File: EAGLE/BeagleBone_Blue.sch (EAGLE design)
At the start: 302 parts, among them J2 SERVO_HEADERS_8X, M1 JST_ZH_2, M2 JST_ZH_2, M3 JST_ZH_2, M4 JST_ZH_2, Q1 MOSFET-N, U1 TCAN1051HV, U10 TXS0108ERGYR, U13 EMMC, U2 SN74LV1T126DBVR, U3 TPD4S012DRY, U4 TPD4S012DRY, U5 24LC_32AT-I/OT, U6 SN74LVC1G07_DCK_5, U7 WL1835MODGBMOCT, U9 TXS0108ERGYR, X2 SCHA5B0200, X3 USB1, X4 10118192-0001LF, Y1 24 MHz, Y2 32.768kHz

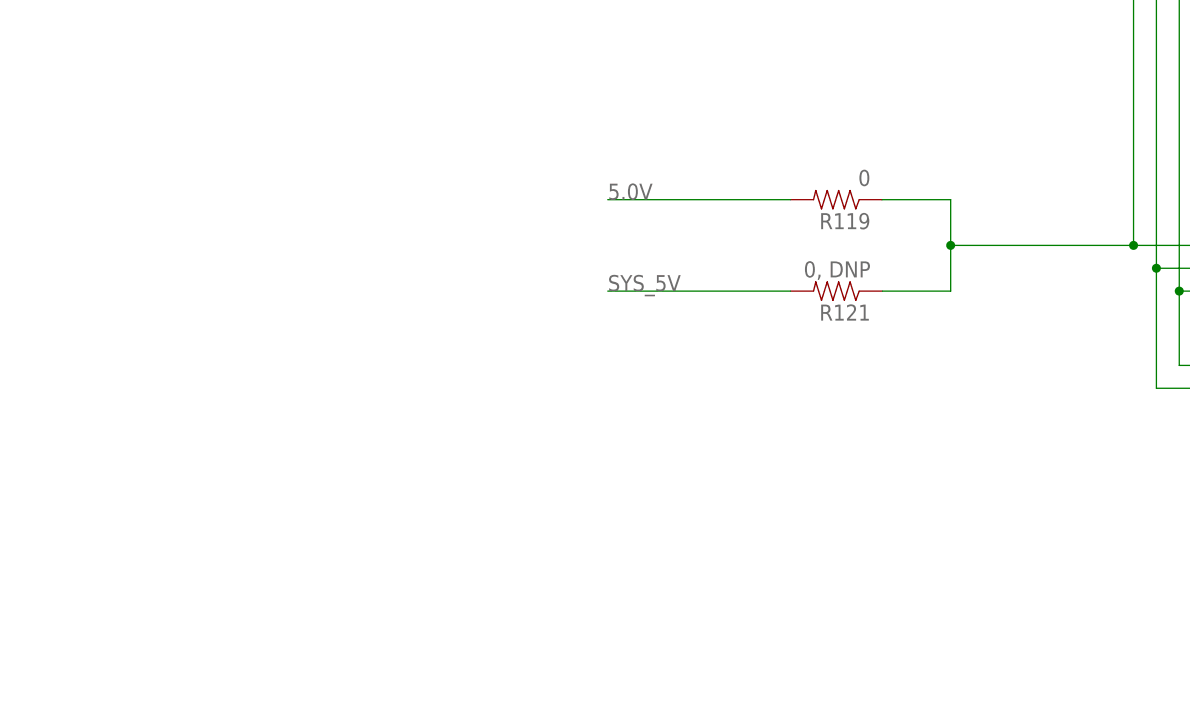
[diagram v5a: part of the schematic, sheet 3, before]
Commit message: Added TPS2105 power mux for USB1 power.
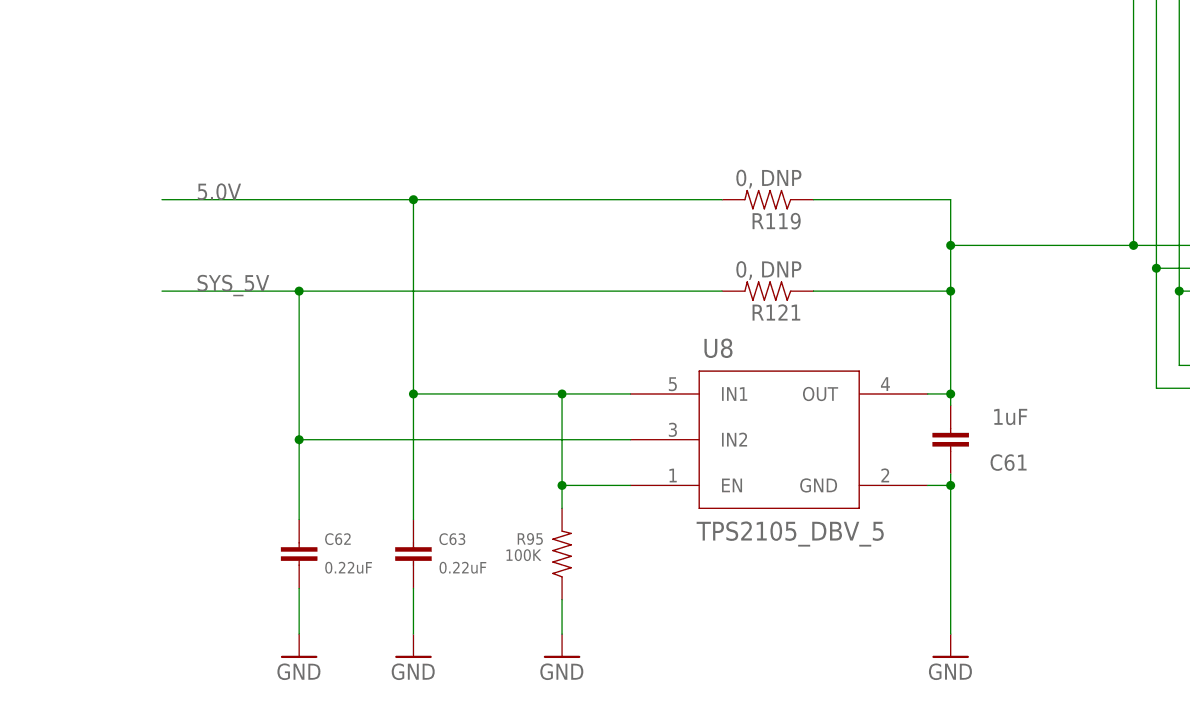
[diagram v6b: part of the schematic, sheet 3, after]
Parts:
- added C61: 1uF, Strawson_Eagle_Lib:CAP0402-CAP
- added C62, C63: 0.22uF, Strawson_Eagle_Lib:CAP0402-CAP
- added R95: 100K, Strawson_Eagle_Lib:RESISTOR0402-RES
- added U8: TPS2105_DBV_5, BeagleBone_Blue:TPS2105_DBV_5
- R119: value 0 -> 0, DNP
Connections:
- net 5.0V: now also C63.1, R95.2, U8.EN, U8.IN1
- net GND: now also C61.1, C62.2, C63.2, R95.1, U8.GND
- net SYS_5V: now also C62.1, U8.IN2
- net USB1_VBUS: now also C61.2, U8.OUT
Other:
- moved on the sheet: R119, R121
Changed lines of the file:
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@@
 <setting verticaltext="up"/>
 </settings>
-<grid distance="0.05" unitdist="inch" unit="inch" style="lines" multiple="1" display="no" altdistance="0.005" altunitdist="inch" altunit="inch"/>
+<grid distance="0.05" unitdist="inch" unit="inch" style="lines" multiple="1" display="no" altdistance="0.01" altunitdist="inch" altunit="inch"/>
 <layers>
 <layer number="1" name="Top" color="4" fill="1" visible="no" active="no"/>
@@
 <part name="R108" library="Strawson_Eagle_Lib" deviceset="RESISTOR" device="0402-RES" value="1K, DNP"/>
 <part name="R104" library="SparkFun-Resistors" deviceset="RESISTOR" device="0603" value="120, DNP"/>
-<part name="R119" library="SparkFun-Resistors" deviceset="RESISTOR" device="0603" value="0"/>
+<part name="R119" library="SparkFun-Resistors" deviceset="RESISTOR" device="0603" value="0, DNP"/>
 <part name="R121" library="SparkFun-Resistors" deviceset="RESISTOR" device="0603" value="0, DNP"/>
 <part name="Y2" library="GHI2" deviceset="CRYSTAL_3.2X1.5" device="" value="32.768kHz"/>
@@
 <part name="C59" library="SparkFun-Capacitors" deviceset="CAP" device="0805" value="10uF"/>
 <part name="C60" library="SparkFun-Capacitors" deviceset="CAP" device="0805" value="10uF"/>
+<part name="U8" library="BeagleBone_Blue" deviceset="TPS2105_DBV_5" device=""/>
+<part name="GND60" library="supply1" deviceset="GND" device=""/>
+<part name="R95" library="Strawson_Eagle_Lib" deviceset="RESISTOR" device="0402-RES" value="100K"/>
+<part name="GND61" library="supply1" deviceset="GND" device=""/>
+<part name="C61" library="Strawson_Eagle_Lib" deviceset="CAP" device="0402-CAP" value="1uF"/>
+<part name="C62" library="Strawson_Eagle_Lib" deviceset="CAP" device="0402-CAP" value="0.22uF"/>
+<part name="C63" library="Strawson_Eagle_Lib" deviceset="CAP" device="0402-CAP" value="0.22uF"/>
+<part name="GND62" library="supply1" deviceset="GND" device=""/>
+<part name="GND63" library="supply1" deviceset="GND" device=""/>
 </parts>
 <sheets>
@@
 <attribute name="VALUE" x="264.414" y="39.116" size="1.778" layer="96"/>
 </instance>
-<instance part="R119" gate="G$1" x="193.04" y="66.04" rot="R180"/>
-<instance part="R121" gate="G$1" x="193.04" y="55.88" rot="R180"/>
+<instance part="R119" gate="G$1" x="185.42" y="66.04" rot="R180"/>
+<instance part="R121" gate="G$1" x="185.42" y="55.88" rot="R180"/>
 <instance part="X4" gate="G$1" x="337.82" y="104.14" smashed="yes">
 <attribute name="NAME" x="332.74" y="115.57" size="1.778" layer="95" font="vector"/>
@@
 <instance part="SUPPLY85" gate="G$1" x="339.09" y="73.66" rot="R180"/>
 <instance part="R112" gate="G$1" x="326.39" y="127" rot="R180"/>
+<instance part="U8" gate="A" x="160.02" y="41.91"/>
+<instance part="GND60" gate="1" x="205.74" y="15.24"/>
+<instance part="R95" gate="G$1" x="162.56" y="26.67" smashed="yes" rot="R90">
+<attribute name="NAME" x="157.48" y="28.3464" size="1.27" layer="95" rot="R180" align="center-right"/>
+<attribute name="VALUE" x="156.21" y="26.543" size="1.27" layer="96" align="center-left"/>
+</instance>
+<instance part="GND61" gate="1" x="162.56" y="15.24"/>
+<instance part="C61" gate="G$1" x="205.74" y="40.64" smashed="yes" rot="R180">
+<attribute name="NAME" x="214.376" y="37.719" size="1.778" layer="95" rot="R180"/>
+<attribute name="VALUE" x="214.376" y="42.799" size="1.778" layer="96" rot="R180"/>
+</instance>
+<instance part="C62" gate="G$1" x="133.35" y="25.4" smashed="yes">
+<attribute name="NAME" x="136.144" y="27.686" size="1.27" layer="95"/>
+<attribute name="VALUE" x="136.144" y="24.511" size="1.27" layer="96"/>
+</instance>
+<instance part="C63" gate="G$1" x="146.05" y="25.4" smashed="yes">
+<attribute name="NAME" x="148.844" y="27.686" size="1.27" layer="95"/>
+<attribute name="VALUE" x="148.844" y="24.511" size="1.27" layer="96"/>
+</instance>
+<instance part="GND62" gate="1" x="146.05" y="15.24"/>
+<instance part="GND63" gate="1" x="133.35" y="15.24"/>
 </instances>
 <busses>
@@
 <pinref part="C55" gate="G$1" pin="2"/>
 </segment>
+<segment>
+<pinref part="U8" gate="A" pin="GND"/>
+<wire x1="203.2" y1="34.29" x2="205.74" y2="34.29" width="0.1524" layer="91"/>
+<wire x1="205.74" y1="34.29" x2="205.74" y2="17.78" width="0.1524" layer="91"/>
+<pinref part="GND60" gate="1" pin="GND"/>
+<pinref part="C61" gate="G$1" pin="1"/>
+<wire x1="205.74" y1="35.56" x2="205.74" y2="34.29" width="0.1524" layer="91"/>
+<junction x="205.74" y="34.29"/>
+</segment>
+<segment>
+<pinref part="GND61" gate="1" pin="GND"/>
+<pinref part="R95" gate="G$1" pin="1"/>
+<wire x1="162.56" y1="17.78" x2="162.56" y2="21.59" width="0.1524" layer="91"/>
+</segment>
+<segment>
+<pinref part="GND63" gate="1" pin="GND"/>
+<pinref part="C62" gate="G$1" pin="2"/>
+<wire x1="133.35" y1="17.78" x2="133.35" y2="22.86" width="0.1524" layer="91"/>
+</segment>
+<segment>
+<pinref part="GND62" gate="1" pin="GND"/>
+<pinref part="C63" gate="G$1" pin="2"/>
+<wire x1="146.05" y1="17.78" x2="146.05" y2="22.86" width="0.1524" layer="91"/>
+</segment>
 </net>
 <net name="GNDA_ADC" class="0">
@@
 <net name="5.0V" class="3">
 <segment>
-<wire x1="187.96" y1="66.04" x2="167.64" y2="66.04" width="0.1524" layer="91"/>
-<label x="167.64" y="66.04" size="1.778" layer="95"/>
+<wire x1="180.34" y1="66.04" x2="146.05" y2="66.04" width="0.1524" layer="91"/>
+<label x="121.92" y="66.04" size="1.778" layer="95"/>
 <pinref part="R119" gate="G$1" pin="2"/>
+<pinref part="U8" gate="A" pin="IN1"/>
+<wire x1="146.05" y1="66.04" x2="118.11" y2="66.04" width="0.1524" layer="91"/>
+<wire x1="170.18" y1="44.45" x2="162.56" y2="44.45" width="0.1524" layer="91"/>
+<wire x1="162.56" y1="44.45" x2="146.05" y2="44.45" width="0.1524" layer="91"/>
+<wire x1="146.05" y1="44.45" x2="146.05" y2="66.04" width="0.1524" layer="91"/>
+<junction x="146.05" y="66.04"/>
+<pinref part="U8" gate="A" pin="EN"/>
+<wire x1="170.18" y1="34.29" x2="162.56" y2="34.29" width="0.1524" layer="91"/>
+<pinref part="R95" gate="G$1" pin="2"/>
+<wire x1="162.56" y1="31.75" x2="162.56" y2="34.29" width="0.1524" layer="91"/>
+<wire x1="162.56" y1="34.29" x2="162.56" y2="44.45" width="0.1524" layer="91"/>
+<junction x="162.56" y="44.45"/>
+<junction x="162.56" y="34.29"/>
+<pinref part="C63" gate="G$1" pin="1"/>
+<wire x1="146.05" y1="30.48" x2="146.05" y2="44.45" width="0.1524" layer="91"/>
+<junction x="146.05" y="44.45"/>
 </segment>
 </net>
 <net name="SYS_5V" class="3">
 <segment>
-<wire x1="187.96" y1="55.88" x2="167.64" y2="55.88" width="0.1524" layer="91"/>
-<label x="167.64" y="55.88" size="1.778" layer="95"/>
+<wire x1="180.34" y1="55.88" x2="133.35" y2="55.88" width="0.1524" layer="91"/>
+<label x="121.92" y="55.88" size="1.778" layer="95"/>
 <pinref part="R121" gate="G$1" pin="2"/>
+<pinref part="U8" gate="A" pin="IN2"/>
+<wire x1="133.35" y1="55.88" x2="118.11" y2="55.88" width="0.1524" layer="91"/>
+<wire x1="170.18" y1="39.37" x2="133.35" y2="39.37" width="0.1524" layer="91"/>
+<wire x1="133.35" y1="39.37" x2="133.35" y2="55.88" width="0.1524" layer="91"/>
+<junction x="133.35" y="55.88"/>
+<pinref part="C62" gate="G$1" pin="1"/>
+<wire x1="133.35" y1="30.48" x2="133.35" y2="39.37" width="0.1524" layer="91"/>
+<junction x="133.35" y="39.37"/>
 </segment>
 </net>
@@
 <wire x1="261.62" y1="47.625" x2="261.62" y2="45.085" width="0.1524" layer="91"/>
 <junction x="261.62" y="47.625"/>
-<wire x1="198.12" y1="66.04" x2="205.74" y2="66.04" width="0.1524" layer="91"/>
+<wire x1="190.5" y1="66.04" x2="205.74" y2="66.04" width="0.1524" layer="91"/>
 <wire x1="205.74" y1="66.04" x2="205.74" y2="60.96" width="0.1524" layer="91"/>
 <wire x1="205.74" y1="60.96" x2="205.74" y2="55.88" width="0.1524" layer="91"/>
-<wire x1="205.74" y1="55.88" x2="198.12" y2="55.88" width="0.1524" layer="91"/>
+<wire x1="205.74" y1="55.88" x2="190.5" y2="55.88" width="0.1524" layer="91"/>
 <junction x="205.74" y="60.96"/>
 <wire x1="226.06" y1="60.96" x2="261.62" y2="60.96" width="0.1524" layer="91"/>
@@
 <pinref part="R121" gate="G$1" pin="1"/>
 <label x="236.22" y="60.96" size="1.778" layer="95"/>
+<pinref part="U8" gate="A" pin="OUT"/>
+<wire x1="203.2" y1="44.45" x2="205.74" y2="44.45" width="0.1524" layer="91"/>
+<wire x1="205.74" y1="44.45" x2="205.74" y2="55.88" width="0.1524" layer="91"/>
+<junction x="205.74" y="55.88"/>
+<pinref part="C61" gate="G$1" pin="2"/>
+<wire x1="205.74" y1="43.18" x2="205.74" y2="44.45" width="0.1524" layer="91"/>
+<junction x="205.74" y="44.45"/>
 </segment>
 </net>

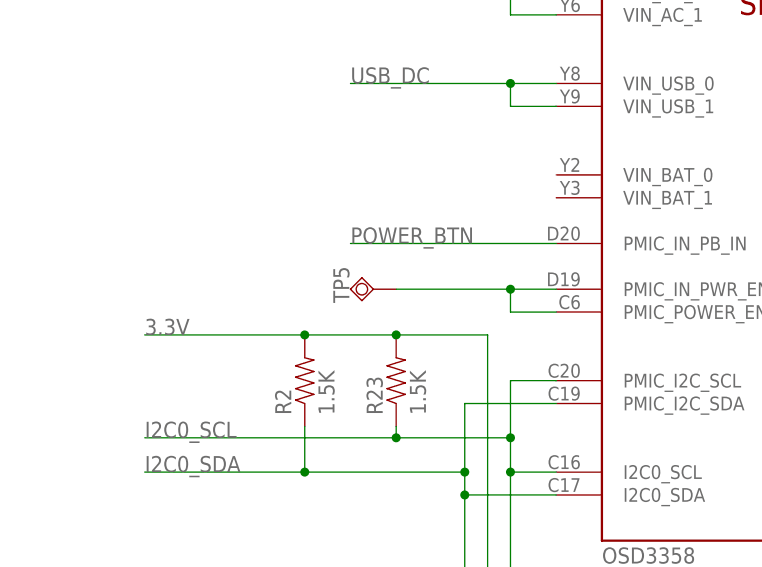
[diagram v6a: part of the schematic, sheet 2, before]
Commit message: Intermediate commit; Updated layout; Fixed TPS2105 footprint.
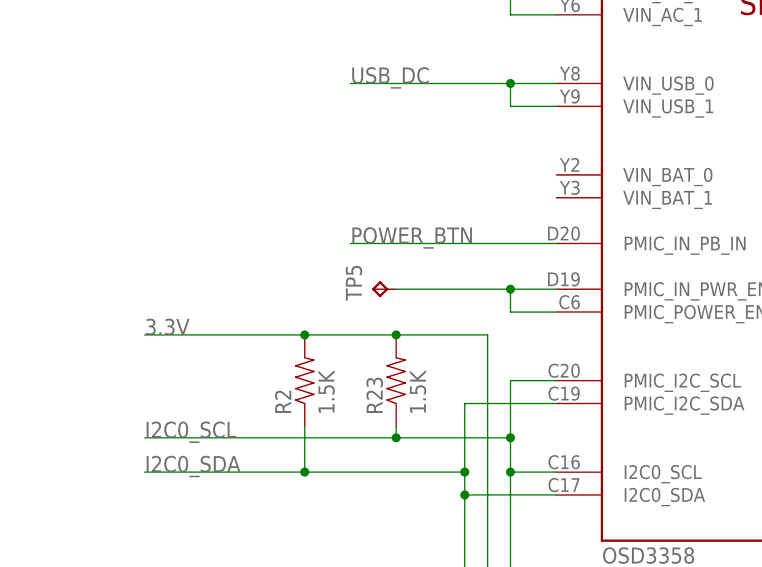
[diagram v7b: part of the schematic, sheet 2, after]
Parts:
- TP5: value TPSQB1,27 -> TPB0,65; device testpad:TPSQB1,27 -> BeagleBone_Blue:TPB0,65
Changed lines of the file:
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@@
 <part name="SIP" library="BeagleBone_Blue" deviceset="OSD3358" device=""/>
 <part name="TP1" library="testpad" deviceset="TPSQ" device="B1,27"/>
-<part name="TP5" library="testpad" deviceset="TPSQ" device="B1,27"/>
 <part name="R2" library="Strawson_Eagle_Lib" deviceset="RESISTOR" device="0402-RES" value="1.5K"/>
 <part name="R23" library="Strawson_Eagle_Lib" deviceset="RESISTOR" device="0402-RES" value="1.5K"/>
@@
 <part name="C59" library="SparkFun-Capacitors" deviceset="CAP" device="0805" value="10uF"/>
 <part name="C60" library="SparkFun-Capacitors" deviceset="CAP" device="0805" value="10uF"/>
-<part name="U8" library="BeagleBone_Blue" deviceset="TPS2105_DBV_5" device=""/>
 <part name="GND60" library="supply1" deviceset="GND" device=""/>
 <part name="R95" library="Strawson_Eagle_Lib" deviceset="RESISTOR" device="0402-RES" value="100K"/>
@@
 <part name="GND62" library="supply1" deviceset="GND" device=""/>
 <part name="GND63" library="supply1" deviceset="GND" device=""/>
+<part name="TP5" library="BeagleBone_Blue" deviceset="TP" device="B0,65"/>
+<part name="U8" library="BeagleBone_Blue" deviceset="TPS2105_DBV_5" device=""/>
 </parts>
 <sheets>
@@
 <instance part="SIP" gate="A" x="71.12" y="182.88"/>
 <instance part="TP1" gate="G$1" x="137.16" y="243.84" rot="R90"/>
-<instance part="TP5" gate="G$1" x="45.72" y="210.82" rot="R270"/>
 <instance part="R2" gate="G$1" x="38.1" y="200.66" rot="R90"/>
 <instance part="R23" gate="G$1" x="48.26" y="200.66" rot="R90"/>
@@
 <instance part="TP11" gate="G$1" x="139.7" y="185.42" rot="R270"/>
 <instance part="GND" gate="G$1" x="38.1" y="151.13" rot="R180"/>
+<instance part="TP5" gate="G$1" x="45.72" y="210.82" rot="R90"/>
 </instances>
 <busses>
@@
 <instance part="SUPPLY85" gate="G$1" x="339.09" y="73.66" rot="R180"/>
 <instance part="R112" gate="G$1" x="326.39" y="127" rot="R180"/>
-<instance part="U8" gate="A" x="160.02" y="41.91"/>
 <instance part="GND60" gate="1" x="205.74" y="15.24"/>
 <instance part="R95" gate="G$1" x="162.56" y="26.67" smashed="yes" rot="R90">
@@
 <instance part="GND62" gate="1" x="146.05" y="15.24"/>
 <instance part="GND63" gate="1" x="133.35" y="15.24"/>
+<instance part="U8" gate="A" x="160.02" y="41.91"/>
 </instances>
 <busses>
@@
 </segment>
 <segment>
-<pinref part="U8" gate="A" pin="GND"/>
 <wire x1="203.2" y1="34.29" x2="205.74" y2="34.29" width="0.1524" layer="91"/>
 <wire x1="205.74" y1="34.29" x2="205.74" y2="17.78" width="0.1524" layer="91"/>
@@
 <wire x1="205.74" y1="35.56" x2="205.74" y2="34.29" width="0.1524" layer="91"/>
 <junction x="205.74" y="34.29"/>
+<pinref part="U8" gate="A" pin="GND"/>
 </segment>
 <segment>
@@
 <label x="121.92" y="66.04" size="1.778" layer="95"/>
 <pinref part="R119" gate="G$1" pin="2"/>
-<pinref part="U8" gate="A" pin="IN1"/>
 <wire x1="146.05" y1="66.04" x2="118.11" y2="66.04" width="0.1524" layer="91"/>
 <wire x1="170.18" y1="44.45" x2="162.56" y2="44.45" width="0.1524" layer="91"/>
@@
 <wire x1="146.05" y1="44.45" x2="146.05" y2="66.04" width="0.1524" layer="91"/>
 <junction x="146.05" y="66.04"/>
-<pinref part="U8" gate="A" pin="EN"/>
 <wire x1="170.18" y1="34.29" x2="162.56" y2="34.29" width="0.1524" layer="91"/>
 <pinref part="R95" gate="G$1" pin="2"/>
@@
 <wire x1="146.05" y1="30.48" x2="146.05" y2="44.45" width="0.1524" layer="91"/>
 <junction x="146.05" y="44.45"/>
+<pinref part="U8" gate="A" pin="EN"/>
+<pinref part="U8" gate="A" pin="IN1"/>
 </segment>
 </net>
@@
 <label x="121.92" y="55.88" size="1.778" layer="95"/>
 <pinref part="R121" gate="G$1" pin="2"/>
-<pinref part="U8" gate="A" pin="IN2"/>
 <wire x1="133.35" y1="55.88" x2="118.11" y2="55.88" width="0.1524" layer="91"/>
 <wire x1="170.18" y1="39.37" x2="133.35" y2="39.37" width="0.1524" layer="91"/>
@@
 <wire x1="133.35" y1="30.48" x2="133.35" y2="39.37" width="0.1524" layer="91"/>
 <junction x="133.35" y="39.37"/>
+<pinref part="U8" gate="A" pin="IN2"/>
 </segment>
 </net>
@@
 <pinref part="R121" gate="G$1" pin="1"/>
 <label x="236.22" y="60.96" size="1.778" layer="95"/>
-<pinref part="U8" gate="A" pin="OUT"/>
 <wire x1="203.2" y1="44.45" x2="205.74" y2="44.45" width="0.1524" layer="91"/>
 <wire x1="205.74" y1="44.45" x2="205.74" y2="55.88" width="0.1524" layer="91"/>
@@
 <wire x1="205.74" y1="43.18" x2="205.74" y2="44.45" width="0.1524" layer="91"/>
 <junction x="205.74" y="44.45"/>
+<pinref part="U8" gate="A" pin="OUT"/>
 </segment>
 </net>
